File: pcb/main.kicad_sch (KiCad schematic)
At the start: 11 parts, among them Q1 S8050, U1 LF356N, U2 LF356N

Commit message: Updated schematic.
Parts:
- removed Q1: S8050, symbol Device:Q_NPN_BCE
- removed RV1, RV2: 10k, symbol Device:R_Potentiometer
- removed U1, U2: LF356N, symbol deps:LF356N
- added C1, C2, C3, C4: 1u, symbol Device:C
- added C6, C7, C8, C9: 4n7, symbol Device:C
- added Q1: BC337, Package_TO_SOT_THT:TO-92_Inline, symbol Transistor_BJT:BC337
- added R1: 1k, symbol Device:R
- added R10, R12, R14, R8: 330, symbol Device:R
- added R11, R13, R7, R9: 5k, symbol Device:R
- added R16: 6k8, symbol Device:R
- added R17, R18, R19, R20: 150, symbol Device:R
- added R2, R6: 10k, symbol Device:R
- added U1, U4: LM358, symbol Amplifier_Operational:LM358
- added U2, U3: LF356N, symbol deps:LF356N_flipped
- R15: renamed from R4; value 390k -> 680k
- R4: renamed from R2; value 32k -> 20k
- R5: renamed from R3; value 830k -> 1M
- renumbered C1 to C5, R1 to R3
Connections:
- net +5V: now also R6.2, U1.8 (V+), U2.7, U3.7, U4.8 (V+)
- net GND: now also C6.2, C7.2, C8.2, C9.2, Q1.3 (E), R16.1, R17.1, R18.1, R19.1, R20.1, U1.4 (V-), U2.4, U3.4, U4.4 (V-)
- net OUTPUT: now also C4.2, R20.2, U4.6 (-), U4.7
- net at C5.2, R15.1, R5.2: now also U1.3 (+)
- net at D1.2 (A): now also Q1.2 (B)
- net at C5.1, R4.2: now also Q1.1 (C)
- new net: R1.1, U1.1, U1.2 (-)
- new net: C3.2, R13.1, R19.2, U4.1, U4.2 (-)
- new net: C8.1, R12.2, U4.3 (+)
- new net: C3.1, R11.2, R12.1
- new net: C1.2, R17.2, R9.1, U2.2 (-), U2.6
- new net: C1.1, R7.2, R8.1
- new net: R16.2, R6.1, U1.5 (+)
- new net: C9.1, R14.2, U4.5 (+)
- new net: R1.2, R2.1, U1.6 (-)
- new net: R2.2, R7.1, U1.7
- new net: C2.2, R11.1, R18.2, U3.2 (-), U3.6
- new net: C7.1, R10.2, U3.3 (+)
- new net: C2.1, R10.1, R9.2
- new net: C4.1, R13.2, R14.1
- new net: C6.1, R8.2, U2.3 (+)
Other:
- moved on the sheet: C5, D1, R15, R3, R4, R5

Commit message: Updated schematic.
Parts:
- removed C1, C2: 1u, symbol Device:C
- removed R10: 330, symbol Device:R
- removed R9: 5k, symbol Device:R
- removed U2, U3: LF356N, symbol deps:LF356N_flipped
- added C10, C11: 4n7, symbol Device:C
- added C12, C13: 10n, symbol Device:C
- added C16, C17: 2.2u, symbol Device:C
- added D2, D3: D_Schottky, symbol Device:D_Schottky
- added R21: 3k2, symbol Device:R
- added R22: 400, symbol Device:R
- added R23, R24: 68k, symbol Device:R
- added R25, R26: 1M, symbol Device:R
- added U5, U6, U7: LM358, symbol Amplifier_Operational:LM358
- C6, C7: value 4n7 -> 1u
- C8, C9: value 4n7 -> 1n
- R11, R13: value 5k -> 280
- R12, R14: value 330 -> 11k22
- R17: value 150 -> 2k6
- R18: value 150 -> 400
- R7: value 5k -> 100k
- R8: value 330 -> 100k
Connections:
- net +5V: now also R7.1, R8.1, U5.8 (V+), U6.8 (V+), U7.8 (V+)
- net GND: now also C10.2, C11.2, C12.2, C13.2, R23.2, R24.2, R25.2, R26.2, U5.4 (V-), U6.4 (V-), U7.4 (V-); no longer C6.2, C7.2, R17.1, R18.1
- net at R17.2: now also C6.1, R18.1
- net at R7.2: now also C16.2, R23.1, U6.5 (+); no longer R8.1
- net at R2.2, U1.7: no longer R7.1
- net at R18.2: now also C10.1, U5.3 (+); no longer R11.1
- net at C7.1: now also R21.2, R22.1
- net at R8.2: now also C17.2, R24.1, U7.5 (+); no longer C6.1
- net OUTPUT: no longer names the net of C4.2, U4.6 (-), U4.7
- net OUTPUT: now also D2.2 (A); no longer R20.2
- new net: C16.1, U6.1, U6.2 (-)
- new net: C12.1, D2.1 (K), R25.1, U6.3 (+)
- new net: C6.2, R20.2, R21.1, U5.1, U5.2 (-)
- new net: C13.1, D3.1 (K), R26.1, U7.3 (+)
- new net: C7.2, D3.2 (A), U5.6 (-), U5.7
- new net: C17.1, U7.1, U7.2 (-)
- new net: C11.1, R22.2, U5.5 (+)
- new net FRONTEND_OUTPUT: R11.1, R17.1
- new net RECTIFIED_2125: U6.6 (-), U6.7
- new net RECTIFIED_2295: U7.6 (-), U7.7
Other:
- note added: "Amplifier/Filter for 2125Hz."
- note added: "Amplifier/Filter for 2295Hz."
- note added: "Rectification & Biasing of 2125Hz."
- note added: "Rectification & Biasing of 2295Hz."
- moved on the sheet: C3, C4, C5, C8, C9, D1, Q1, R1, R11, R12, R15, R16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

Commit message: Updated schematic.
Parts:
- removed C11: 4n7, symbol Device:C
- removed C16, C17: 2.2u, symbol Device:C
- removed C3, C4, C7: 1u, symbol Device:C
- removed C5, C8, C9: 1n, symbol Device:C
- removed D1: LTR-516AD, symbol Device:D_Photo
- removed Q1: BC337, Package_TO_SOT_THT:TO-92_Inline, symbol Transistor_BJT:BC337
- removed R11, R13: 280, symbol Device:R
- removed R12, R14: 11k22, symbol Device:R
- removed R15: 680k, symbol Device:R
- removed R16: 6k8, symbol Device:R
- removed R17: 2k6, symbol Device:R
- removed R18, R22: 400, symbol Device:R
- removed R19, R20: 150, symbol Device:R
- removed R2, R6: 10k, symbol Device:R
- removed R21: 3k2, symbol Device:R
- removed R23, R24: 68k, symbol Device:R
- removed R3: 330, symbol Device:R
- removed R4: 20k, symbol Device:R
- removed R5: 1M, symbol Device:R
- removed R7, R8: 100k, symbol Device:R
- removed unit 3 of U1
- removed U4, U5, U7: LM358, symbol Amplifier_Operational:LM358
- removed unit 2 of U6
- removed unit 3 of U6
- added C1: 1u, symbol Device:C
- added C2: 1n, symbol Device:C
- added D1, D2: 1N5817, symbol Device:D_Schottky
- added R2: 10k, symbol Device:R_Trim
- added R3, R4, R5, R6: 20k, symbol Device:R_Trim
- added RV1: 1k, symbol Device:R_Potentiometer
- added U2, U3: LM358, symbol Amplifier_Operational:LM358
- C5: renamed from C12; value 10n -> 2u
- C6: renamed from C13; value 10n -> 2u
- D3: renamed from D2; value D_Schottky -> 1N5817
- D4: renamed from D3; value D_Schottky -> 1N5817
- R7: renamed from R25; value 1M -> 100k
- R8: renamed from R26; value 1M -> 100k
- renumbered C6 to C3, C10 to C4, U6 to U4
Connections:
- net +5V: now also RV1.1
- net FRONTEND_OUTPUT: now also R1.1
- net GND: now also C2.2, R2.2
- net at C3.1: now also R4.2, R6.1
- net at U4.2 (-): now also C6.1, D4.1 (K), R8.1; no longer U4.1
- net at U1.3 (+): now also RV1.2
- net at C3.2: now also D4.2 (A), U3.6 (-), U3.7
- net at C4.1: now also R6.2, U3.5 (+)
- net at D3.2 (A): now also C1.2, U3.1, U3.2 (-)
- net at U1.5 (+): now also R2.1, RV1.3
- net at R1.2, U1.6 (-): now also U1.2 (-), D1.2 (A), D2.1 (K), U2.3 (+)
- net at U1.7: now also D2.2 (A)
- new net: C2.1, R5.2, U3.3 (+)
- new net: D1.1 (K), U1.1
- new net: R3.1, R4.1, U2.1, U2.2 (-)
- new net: C1.1, R3.2, R5.1
- new net DECODED_SIGNAL: U4.1
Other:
- note added: "Clipping."
- note added: "Rectification & Differentiation."
- note removed: "Rectification & Biasing of 2125Hz."
- note removed: "Rectification & Biasing of 2295Hz."
- moved on the sheet: C3, C4, C5, C6, D3, D4, R7, R8, U4A

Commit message: Updated schematic.
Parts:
- added A1: Arduino Nano, Module:Arduino_Nano, symbol MCU_Module:Arduino_Nano_v3.x
- added C1: 1n, symbol Device:C
- added C10, C11, C12, C13: 4n7, symbol Device:C
- added C2, C3, C4, C5, C6, C7: 100n, symbol Device:C_Small
- added C8: 1u, symbol Device:C
- added C9: 10u, symbol Device:C
- added D1: IR1503, symbol Device:D_Photo
- added J1: Aluminum, symbol Device:RFShield_OnePiece
- added L1: 20mH, symbol Device:L
- added Q1: BC337, Package_TO_SOT_THT:TO-92_Inline, symbol Transistor_BJT:BC337
- added R1: 200k, symbol Device:R_Trim
- added R10, R6, R7, R9: 15k, symbol Device:R
- added R11, R8: 33k, symbol Device:R
- added R2: 680k, symbol Device:R
- added R3: 1M, symbol Device:R
- added R4: 680, symbol Device:R
- added R5: 330, symbol Device:R
- added RV1: 200, symbol Device:R_Potentiometer
- added RV2: 100k, symbol Device:R_Potentiometer
- added U1, U2: LM358, symbol Amplifier_Operational:LM358
- added unit 3 of U3
- added unit 2 of U4
- added unit 3 of U4
- added unit 3 of U5
- added unit 3 of U6
- added unit 2 of U6
- renumbered C1 to C14, C2 to C15, C3 to C16, C4 to C17, C5 to C18, C6 to C19, D1 to D2, D2 to D3, D3 to D4, D4 to D5, R1 to R12, R2 to R13, R3 to R14, R4 to R15, R5 to R16, R6 to R17, R7 to R18, R8 to R19, RV1 to RV3, U1 to U3, U2 to U4, U3 to U5, U4 to U6
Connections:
- net +5V: now also A1.27 (+5V), L1.1, U6.8 (V+); no longer RV3.1
- net GND: now also A1.29 (GND), A1.4 (GND), C2.2, C3.2, C4.2, C5.2, C6.2, C7.2, C8.2, C9.2, J1.1 (Shield), Q1.3 (E), R10.2, R3.2, R5.2, R7.2, U1.4 (V-), U2.4 (V-), U3.4 (V-), U4.4 (V-), U4.6 (-), U5.4 (V-), U6.4 (V-), U6.6 (-)
- net DECODED_SIGNAL renamed signal
- net signal: now also A1.9 (D6)
- net FRONTEND_OUTPUT: no longer names the net of R12.1
- net FRONTEND_OUTPUT: now also C12.2, R11.1, U2.7
- new net: C13.2, R11.2, U2.5 (+)
- new net: C12.1, C13.1, R10.1, R9.1
- new net: C1.1, Q1.1 (C), R1.2
- new net: D1.2 (A), Q1.2 (B)
- new net: RV2.1, U1.1, U1.2 (-)
- new net: C1.2, R2.2, R3.1, U1.3 (+)
- new net: U4.5 (+), U4.7
- new net: C10.1, C11.1, R6.1, R7.1
- new net: R6.2, RV2.3, U1.7
- new net: RV1.2, U1.5 (+), U2.2 (-), U2.6 (-)
- new net: R4.2, RV1.1
- new net: RV2.2, U1.6 (-)
- new net: R5.1, RV1.3
- new net: C11.2, R8.2, U2.3 (+)
- new net: C10.2, R8.1, R9.2, U2.1
- new net: U6.5 (+), U6.7
- new net +5VA: C2.1, C3.1, C4.1, C5.1, C6.1, C7.1, C8.1, C9.1, D1.1 (K), L1.2, R1.1, R2.1, R4.1, RV3.1, U1.8 (V+), U2.8 (V+), U3.8 (V+), U4.8 (V+), U5.8 (V+)
- no-connect marks 0 -> 26
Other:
- note added: "Amplifier for 2125Hz."
- note added: "Amplifier for 2295Hz."
- note added: "Arduino."
- note added: "BJT Amplification."
- note added: "Biasing."
- note added: "Inverting Amplification."
- note added: "Narrowband Filtering."
- note added: "Ref. Voltage."
- note removed: "Amplifier/Filter for 2125Hz."
- note removed: "Amplifier/Filter for 2295Hz."
- moved on the sheet: C14, C15, C16, C17, C18, C19, D2, D3, D4, D5, R12, R13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

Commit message: Beginning to model an actual PCB.
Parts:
- removed A1: Arduino Nano, Module:Arduino_Nano, symbol MCU_Module:Arduino_Nano_v3.x
- removed C1, C15: 1n, symbol Device:C
- removed C10, C11, C12, C13, C17: 4n7, symbol Device:C
- removed C14, C16, C8: 1u, symbol Device:C
- removed C18, C19: 2u, symbol Device:C
- removed C2, C3, C4, C5, C6, C7: 100n, symbol Device:C_Small
- removed C9: 10u, symbol Device:C
- removed D2, D3, D4, D5: 1N5817, symbol Device:D_Schottky
- removed J1: Aluminum, symbol Device:RFShield_OnePiece
- removed L1: 20mH, symbol Device:L
- removed R10, R6, R7, R9: 15k, symbol Device:R
- removed R11, R8: 33k, symbol Device:R
- removed R12: 1k, symbol Device:R
- removed R13: 10k, symbol Device:R_Trim
- removed R14, R15, R16, R17: 20k, symbol Device:R_Trim
- removed R18, R19: 100k, symbol Device:R
- removed R2: 680k, symbol Device:R
- removed R3: 1M, symbol Device:R
- removed R4: 680, symbol Device:R
- removed R5: 330, symbol Device:R
- removed RV1: 200, symbol Device:R_Potentiometer
- removed RV2: 100k, symbol Device:R_Potentiometer
- removed RV3: 1k, symbol Device:R_Potentiometer
- removed U1, U2, U3, U4, U5, U6: LM358, symbol Amplifier_Operational:LM358
- D1: footprint (none) -> deps:LTR-516AD
- R1: value 200k -> 100k; footprint (none) -> deps:Trimmer 3362P
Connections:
- net +5VA is gone; now on net +5V: D1.1 (K), R1.1
- no-connect marks 26 -> 0
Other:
- note removed: "Amplifier for 2125Hz."
- note removed: "Amplifier for 2295Hz."
- note removed: "Arduino."
- note removed: "Biasing."
- note removed: "Clipping."
- note removed: "Inverting Amplification."
- note removed: "Narrowband Filtering."
- note removed: "Rectification & Differentiation."
- note removed: "Ref. Voltage."
- moved on the sheet: D1, Q1, R1

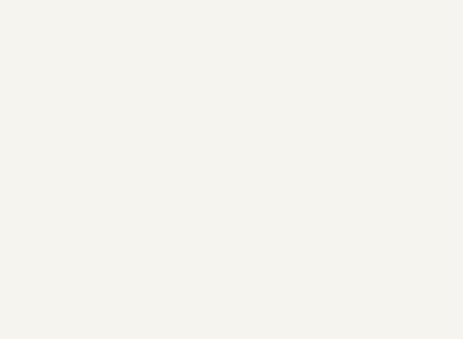
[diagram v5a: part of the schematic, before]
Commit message: Added edge cuts and a model hand for size reference.
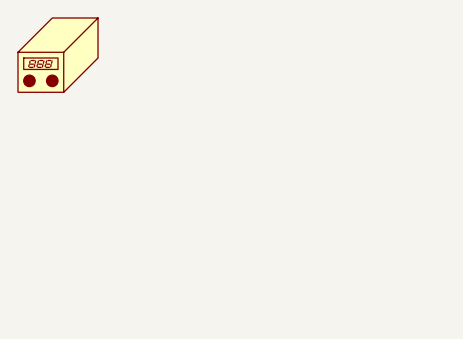
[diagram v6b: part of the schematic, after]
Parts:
- added N1: Housing, deps:Housing - main, symbol Mechanical:Housing
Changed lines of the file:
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@@
+	)
+	(symbol
+		(lib_id "Mechanical:Housing")
+		(at 29.21 31.75 0)
+		(unit 1)
+		(exclude_from_sim no)
+		(in_bom yes)
+		(on_board yes)
+		(dnp no)
+		(fields_autoplaced yes)
+		(property "Reference" "N1"
+			(at 33.02 30.7974 0)
+			(effects
+				(font
+					(size 1.27 1.27)
+				)
+				(justify left)
+				(hide yes)
+			)
+		)
+		(property "Value" "Housing"
+			(at 33.02 33.3374 0)
+			(effects
+				(font
+					(size 1.27 1.27)
+				)
+				(justify left)
+				(hide yes)
+			)
+		)
+		(property "Footprint" "deps:Housing - main"
+			(at 30.48 30.48 0)
+			(effects
+				(font
+					(size 1.27 1.27)
+				)
+				(hide yes)
+			)
+		)
+		(property "Datasheet" "~"
+			(at 30.48 30.48 0)
+			(effects
+				(font
+					(size 1.27 1.27)
+				)
+				(hide yes)
+			)
+		)
+		(property "Description" "Housing"
+			(at 29.21 31.75 0)
+			(effects
+				(font
+					(size 1.27 1.27)
+				)
+				(hide yes)
+			)
+		)
+		(instances
+			(project ""
+				(path "/5b58330d-a0f3-43de-a3af-b429ccd24917"
+					(reference "N1")
+					(unit 1)
+				)
+			)
+		)
 	)
 	(symbol

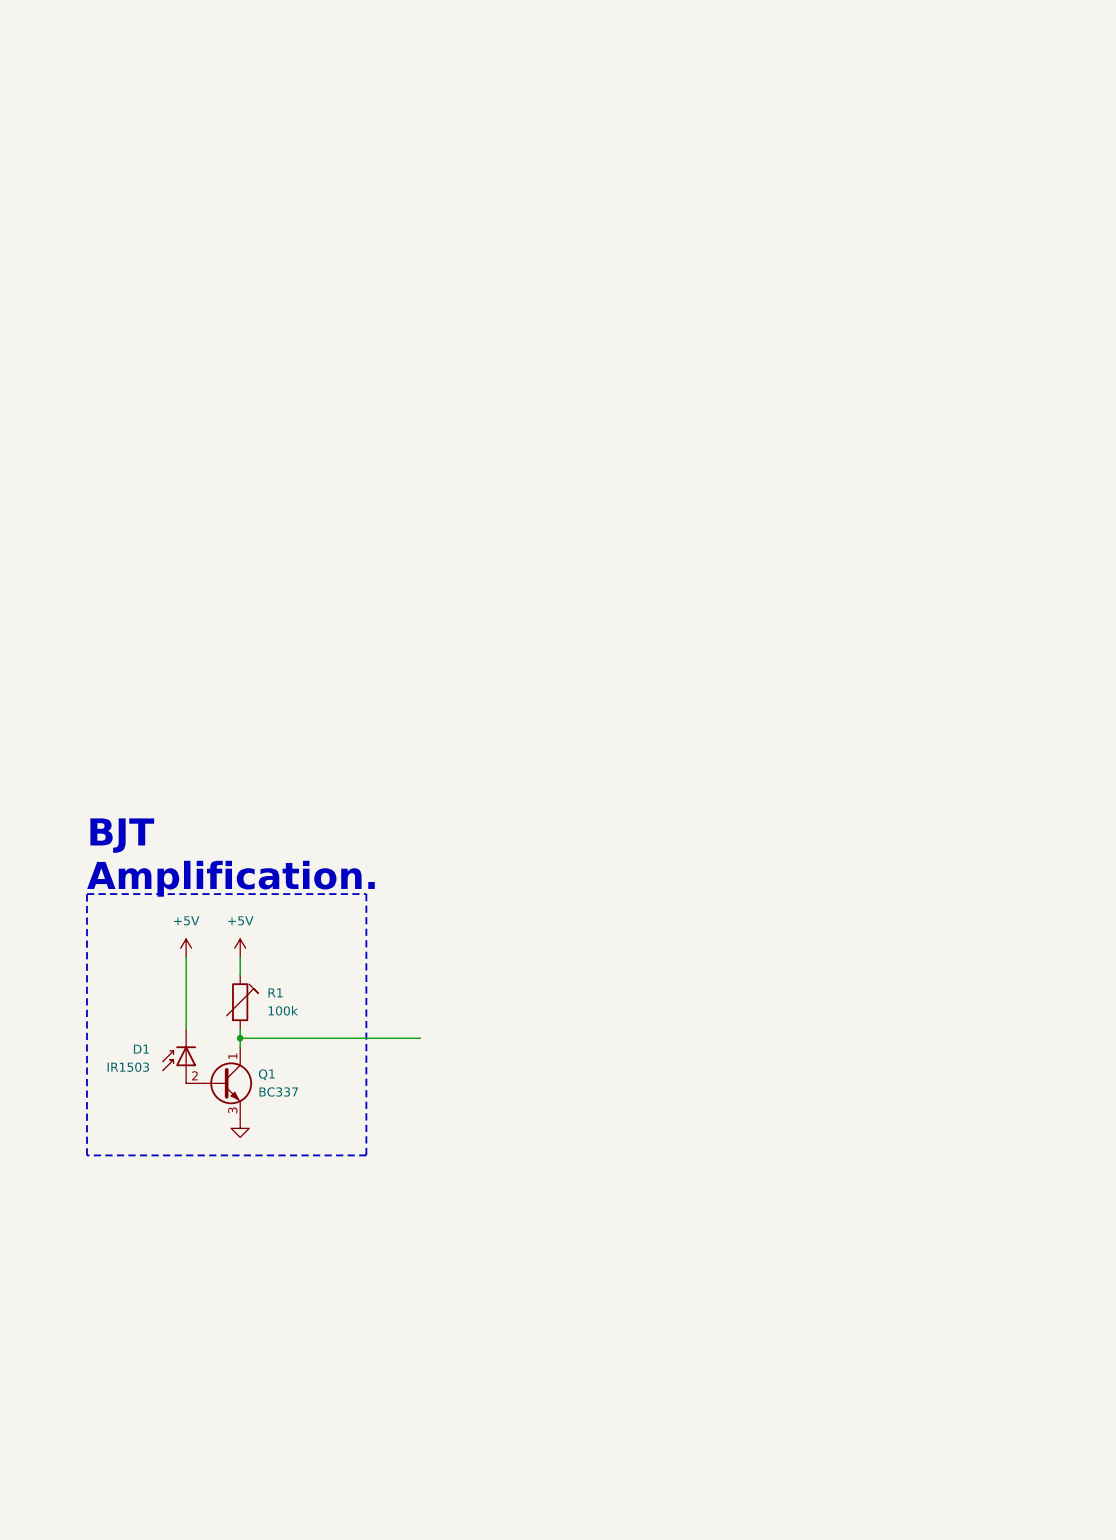
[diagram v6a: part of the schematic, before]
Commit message: Laid out first stages.
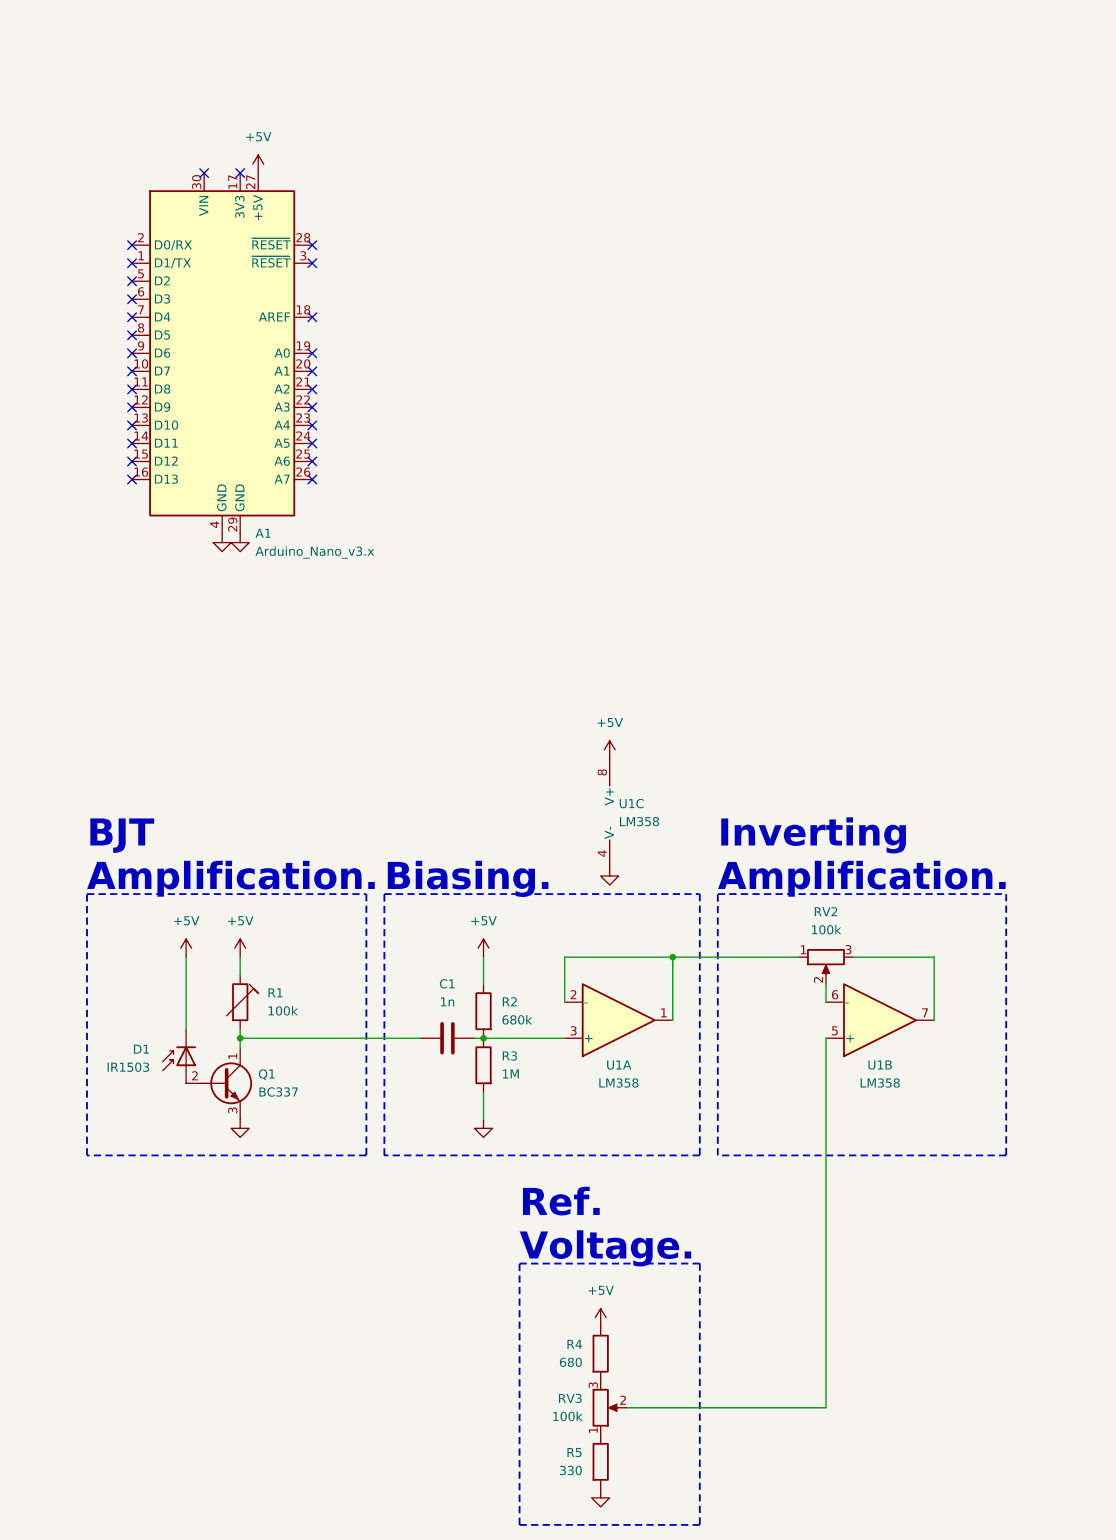
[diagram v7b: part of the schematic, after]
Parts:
- added A1: Arduino_Nano_v3.x, deps:Arduino_Nano, symbol MCU_Module:Arduino_Nano_v3.x
- added C1: 1n, Capacitor_SMD:C_1206_3216Metric_Pad1.33x1.80mm_HandSolder, symbol Device:C
- added R2: 680k, Resistor_SMD:R_1206_3216Metric_Pad1.30x1.75mm_HandSolder, symbol Device:R
- added R3: 1M, Resistor_SMD:R_1206_3216Metric_Pad1.30x1.75mm_HandSolder, symbol Device:R
- added R4: 680, Resistor_SMD:R_1206_3216Metric_Pad1.30x1.75mm_HandSolder, symbol Device:R
- added R5: 330, Resistor_SMD:R_1206_3216Metric_Pad1.30x1.75mm_HandSolder, symbol Device:R
- added RV2, RV3: 100k, deps:Potentiometer 3362P, symbol Device:R_Potentiometer
- added U1: LM358, symbol Amplifier_Operational:LM358
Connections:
- net +5V: now also A1.27 (+5V), R2.1, R4.1, U1.8 (V+)
- net GND: now also A1.29 (GND), A1.4 (GND), R3.2, R5.2, U1.4 (V-)
- net at Q1.1 (C), R1.2: now also C1.1
- new net: R5.1, RV3.1
- new net: RV3.2, U1.5 (+)
- new net: R4.2, RV3.3
- new net: RV2.1, U1.1, U1.2 (-)
- new net: C1.2, R2.2, R3.1, U1.3 (+)
- new net: RV2.2, U1.6 (-)
- new net: RV2.3, U1.7
- no-connect marks 0 -> 27
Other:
- note added: "Biasing."
- note added: "Inverting Amplification."
- note added: "Ref. Voltage."
